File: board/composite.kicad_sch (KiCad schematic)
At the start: 17 parts, among them J6 COMPOSITE, U17 ATF1508ASx-xxJx84, U18 74HC373, U19 74HC373, U20 74HC165, U21 74HC165, Y3 14.318 MHz

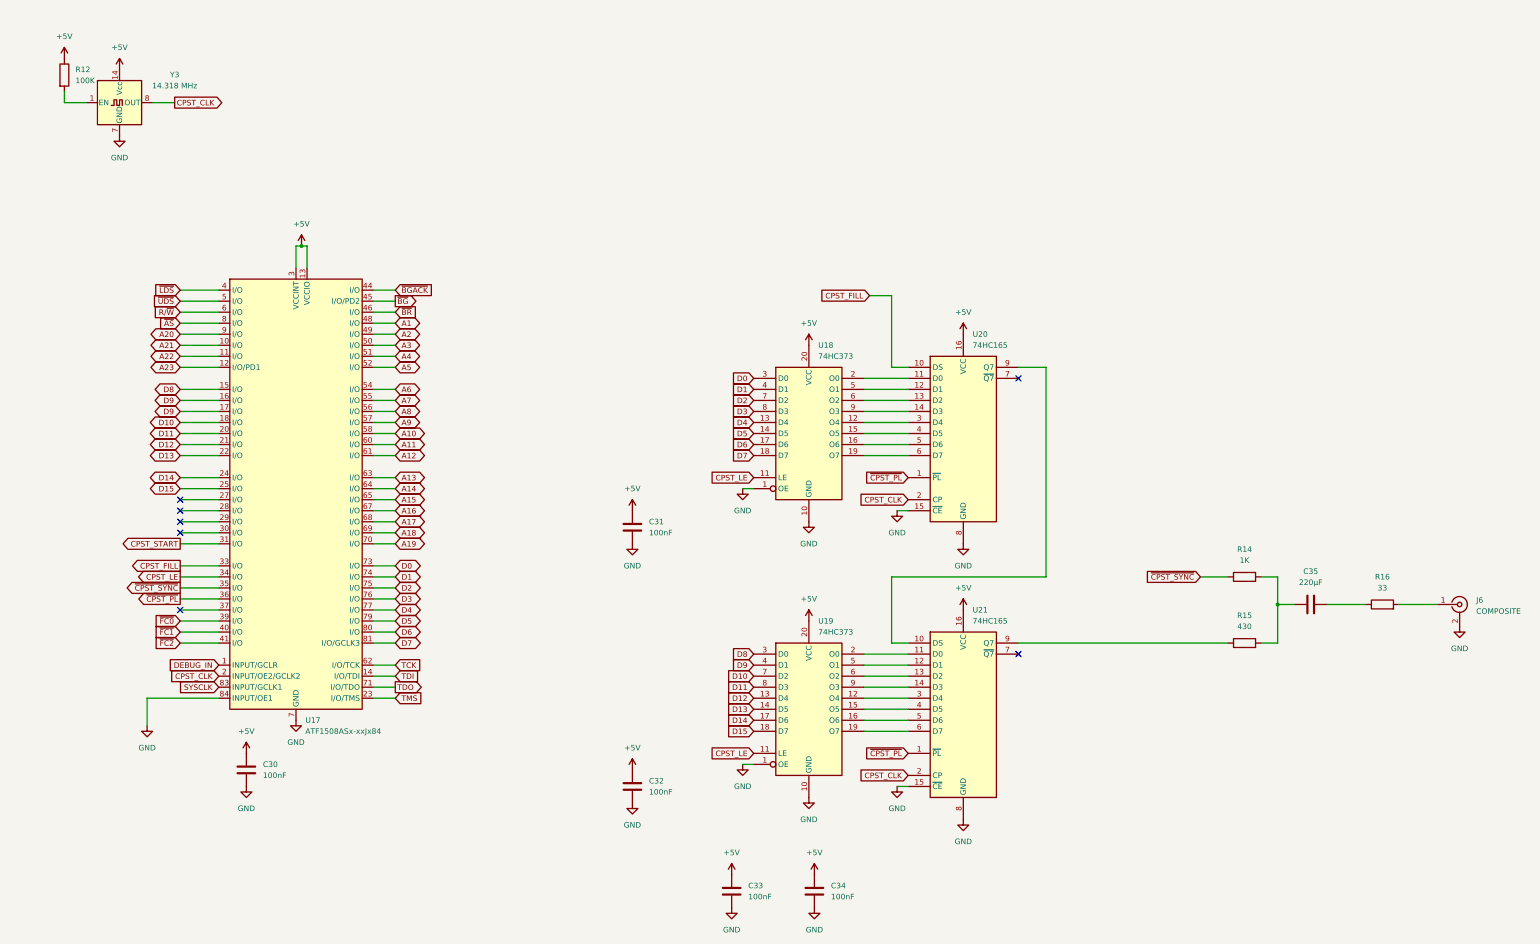
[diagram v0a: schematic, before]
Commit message: change IO to 8051 variant, add audio
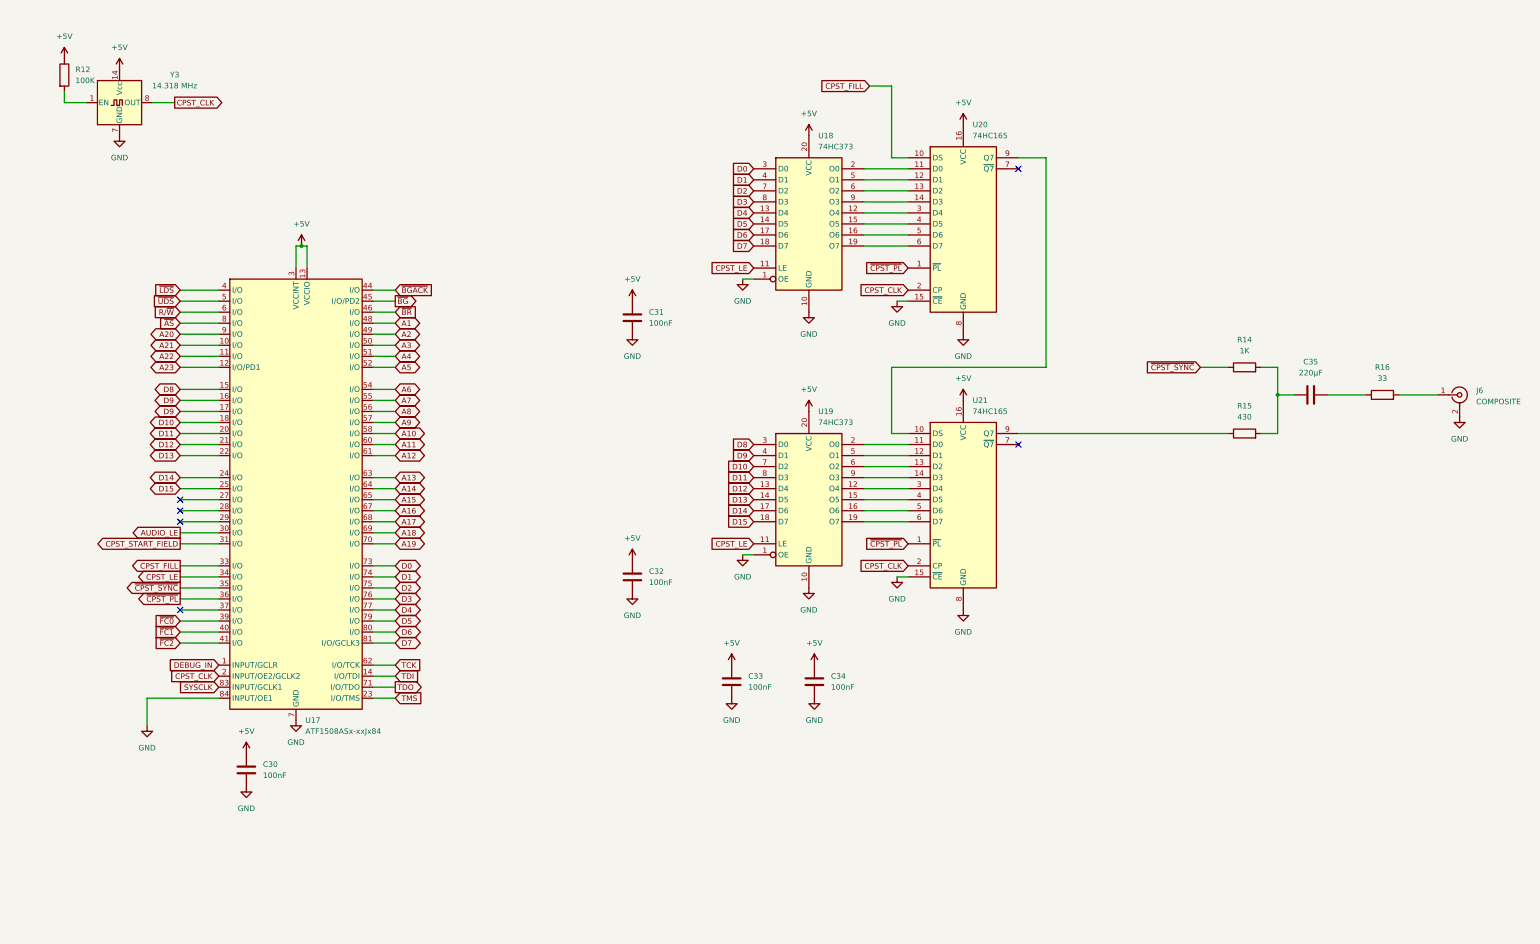
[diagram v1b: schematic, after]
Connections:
- net AUDIO_LE: now reaches U17.30 (I/O)
- net CPST_START renamed CPST_START_FIELD
- no-connect marks 7 -> 6
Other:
- moved on the sheet: C31, C32, C33, C34, C35, J6, R14, R15, R16, U18, U19, U20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

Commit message: design draft complete, added footprints
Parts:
- C30, C31, C32, C33, C34: footprint (none) -> Capacitor_THT:C_Disc_D5.0mm_W2.5mm_P5.00mm
- C35: footprint (none) -> Capacitor_THT:CP_Radial_D6.3mm_P2.50mm
- J6: footprint (none) -> board:CUI_RCJ-044
- R12, R14, R15, R16: footprint (none) -> Resistor_THT:R_Axial_DIN0207_L6.3mm_D2.5mm_P10.16mm_Horizontal
- U18, U19, U20, U21: footprint (none) -> Package_DIP:DIP-20_W7.62mm
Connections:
- net D10: now also U17.17 (I/O); no longer U17.18 (I/O)
- net D11: now also U17.18 (I/O); no longer U17.20 (I/O)
- net D12: now also U17.20 (I/O); no longer U17.21 (I/O)
- net D13: now also U17.21 (I/O); no longer U17.22 (I/O)
- net D14: now also U17.22 (I/O); no longer U17.24 (I/O)
- net D15: now also U17.24 (I/O); no longer U17.25 (I/O)
- net D9: no longer U17.17 (I/O)
- no-connect marks 6 -> 7
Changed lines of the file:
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@@
 	)
 	(no_connect
+		(at 50.8 124.46)
+	)
+	(no_connect
 		(at 50.8 127)
 	)
@@
 	(global_label "D13"
 		(shape bidirectional)
-		(at 50.8 116.84 180)
+		(at 50.8 114.3 180)
 		(fields_autoplaced yes)
 		(effects
@@
 		)
 		(property "Intersheetrefs" "${INTERSHEET_REFS}"
-			(at 44.224 116.84 0)
+			(at 44.224 114.3 0)
 			(effects
 				(font
@@
 		)
 	)
-	(global_label "D9"
-		(shape bidirectional)
-		(at 50.8 104.14 180)
-		(fields_autoplaced yes)
-		(effects
-			(font
-				(size 1.27 1.27)
-			)
-			(justify right)
-		)
-		(property "Intersheetrefs" "${INTERSHEET_REFS}"
-			(at 44.224 104.14 0)
-			(effects
-				(font
-					(size 1.27 1.27)
-				)
-				(justify right)
-				(hide yes)
-			)
-		)
-	)
 	(global_label "A18"
 		(shape bidirectional)
@@
 	(global_label "D14"
 		(shape bidirectional)
-		(at 50.8 121.92 180)
+		(at 50.8 116.84 180)
 		(fields_autoplaced yes)
 		(effects
@@
 		)
 		(property "Intersheetrefs" "${INTERSHEET_REFS}"
-			(at 44.224 121.92 0)
+			(at 44.224 116.84 0)
 			(effects
 				(font
@@
 	(global_label "D15"
 		(shape bidirectional)
-		(at 50.8 124.46 180)
+		(at 50.8 121.92 180)
 		(fields_autoplaced yes)
 		(effects
@@
 		)
 		(property "Intersheetrefs" "${INTERSHEET_REFS}"
-			(at 44.224 124.46 0)
+			(at 44.224 121.92 0)
 			(effects
 				(font
@@
 	(global_label "D11"
 		(shape bidirectional)
-		(at 50.8 111.76 180)
+		(at 50.8 109.22 180)
 		(fields_autoplaced yes)
 		(effects
@@
 		)
 		(property "Intersheetrefs" "${INTERSHEET_REFS}"
-			(at 44.224 111.76 0)
+			(at 44.224 109.22 0)
 			(effects
 				(font
@@
 	(global_label "D10"
 		(shape bidirectional)
-		(at 50.8 109.22 180)
+		(at 50.8 106.68 180)
 		(fields_autoplaced yes)
 		(effects
@@
 		)
 		(property "Intersheetrefs" "${INTERSHEET_REFS}"
-			(at 44.224 109.22 0)
+			(at 44.224 106.68 0)
 			(effects
 				(font
@@
 	(global_label "D9"
 		(shape bidirectional)
-		(at 50.8 106.68 180)
+		(at 50.8 104.14 180)
 		(fields_autoplaced yes)
 		(effects
@@
 		)
 		(property "Intersheetrefs" "${INTERSHEET_REFS}"
-			(at 44.224 106.68 0)
+			(at 44.224 104.14 0)
 			(effects
 				(font
@@
 	(global_label "D12"
 		(shape bidirectional)
-		(at 50.8 114.3 180)
+		(at 50.8 111.76 180)
 		(fields_autoplaced yes)
 		(effects
@@
 		)
 		(property "Intersheetrefs" "${INTERSHEET_REFS}"
-			(at 44.224 114.3 0)
+			(at 44.224 111.76 0)
 			(effects
 				(font
@@
 			)
 		)
-		(property "Footprint" ""
+		(property "Footprint" "Package_DIP:DIP-20_W7.62mm"
 			(at 195.58 63.5 0)
 			(effects
@@
 			)
 		)
-		(property "Footprint" ""
+		(property "Footprint" "Capacitor_THT:CP_Radial_D6.3mm_P2.50mm"
 			(at 314.96 101.9048 0)
 			(effects
@@
 			)
 		)
-		(property "Footprint" ""
+		(property "Footprint" "Resistor_THT:R_Axial_DIN0207_L6.3mm_D2.5mm_P10.16mm_Horizontal"
 			(at 295.91 113.538 90)
 			(effects
@@
 			)
 		)
-		(property "Footprint" ""
+		(property "Footprint" "Capacitor_THT:C_Disc_D5.0mm_W2.5mm_P5.00mm"
 			(at 67.0052 193.04 0)
 			(effects
@@
 			)
 		)
-		(property "Footprint" ""
+		(property "Footprint" "Resistor_THT:R_Axial_DIN0207_L6.3mm_D2.5mm_P10.16mm_Horizontal"
 			(at 327.66 104.648 90)
 			(effects
@@
 			)
 		)
-		(property "Footprint" ""
+		(property "Footprint" "Capacitor_THT:C_Disc_D5.0mm_W2.5mm_P5.00mm"
 			(at 155.9052 88.9 0)
 			(effects
@@
 			)
 		)
-		(property "Footprint" ""
+		(property "Footprint" "Package_DIP:DIP-20_W7.62mm"
 			(at 231.14 127 0)
 			(effects
@@
 			)
 		)
-		(property "Footprint" ""
+		(property "Footprint" "Package_DIP:DIP-20_W7.62mm"
 			(at 231.14 63.5 0)
 			(effects
@@
 			)
 		)
-		(property "Footprint" ""
+		(property "Footprint" "board:CUI_RCJ-044"
 			(at 345.44 102.87 0)
 			(effects
@@
 			)
 		)
-		(property "Footprint" ""
+		(property "Footprint" "Capacitor_THT:C_Disc_D5.0mm_W2.5mm_P5.00mm"
 			(at 197.8152 172.72 0)
 			(effects
@@
 			)
 		)
-		(property "Footprint" ""
+		(property "Footprint" "Package_DIP:DIP-20_W7.62mm"
 			(at 195.58 127 0)
 			(effects
@@
 			)
 		)
-		(property "Footprint" ""
+		(property "Footprint" "Resistor_THT:R_Axial_DIN0207_L6.3mm_D2.5mm_P10.16mm_Horizontal"
 			(at 295.91 98.298 90)
 			(effects
@@
 			)
 		)
-		(property "Footprint" ""
+		(property "Footprint" "Capacitor_THT:C_Disc_D5.0mm_W2.5mm_P5.00mm"
 			(at 155.9052 148.59 0)
 			(effects
@@
 			)
 		)
-		(property "Footprint" ""
+		(property "Footprint" "Resistor_THT:R_Axial_DIN0207_L6.3mm_D2.5mm_P10.16mm_Horizontal"
 			(at 22.352 29.21 90)
 			(effects
@@
 			)
 		)
-		(property "Footprint" ""
+		(property "Footprint" "Capacitor_THT:C_Disc_D5.0mm_W2.5mm_P5.00mm"
 			(at 178.7652 172.72 0)
 			(effects

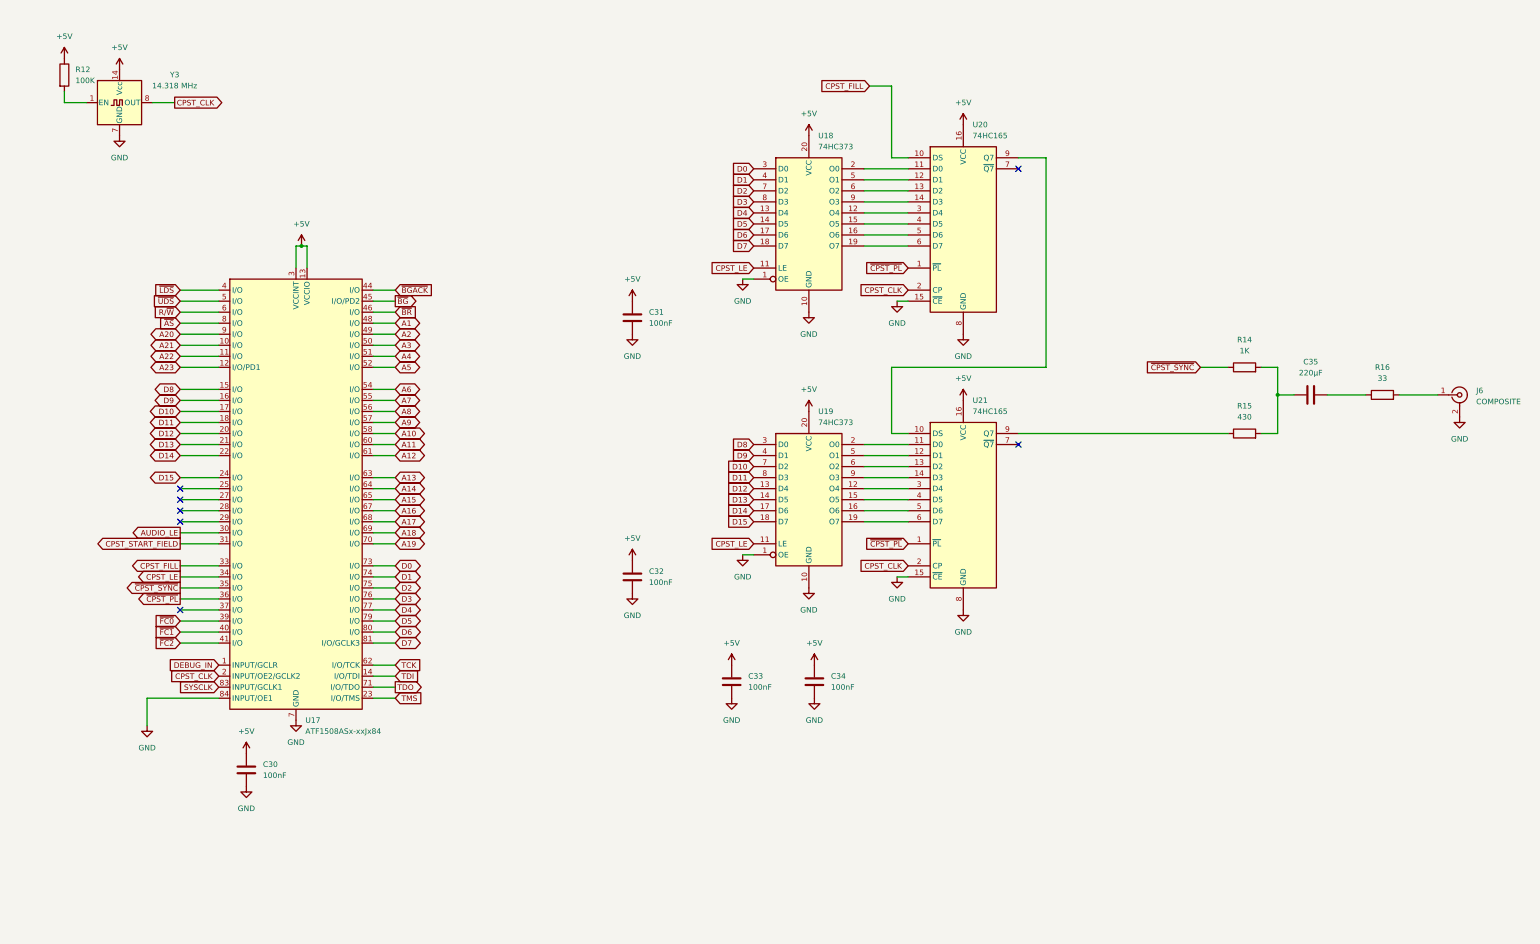
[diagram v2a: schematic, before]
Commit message: start of PCB and MMU
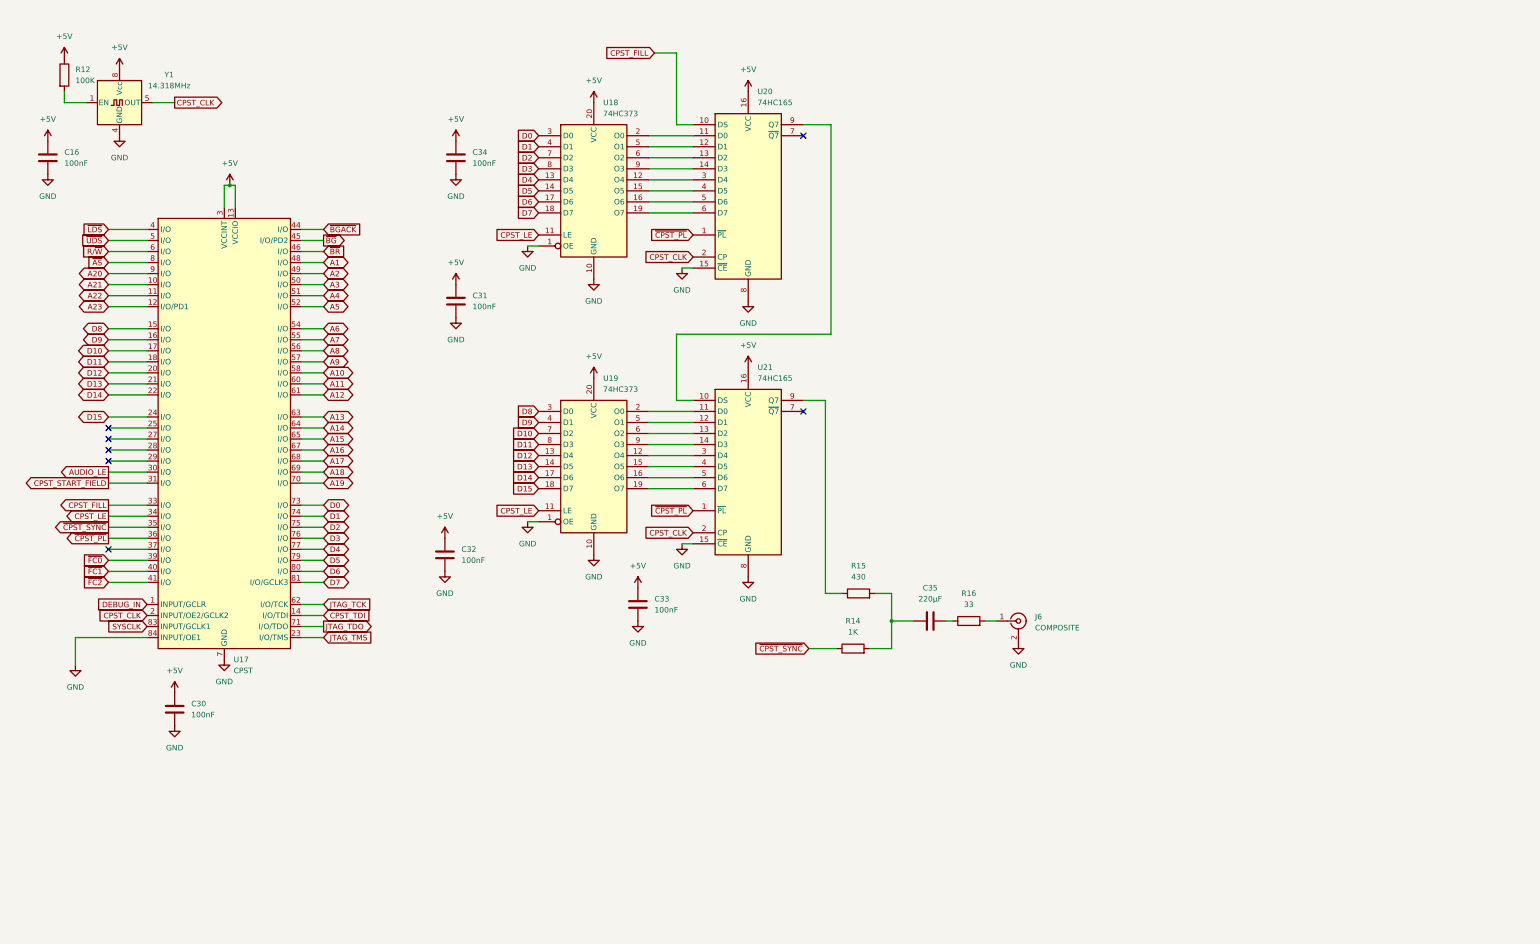
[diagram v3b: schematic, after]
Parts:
- removed Y3: 14.318 MHz, Oscillator:Oscillator_DIP-14, symbol Oscillator:CXO_DIP14
- added C16: 100nF, Capacitor_THT:C_Disc_D5.0mm_W2.5mm_P5.00mm, symbol Device:C
- added Y1: 14.318MHz, Oscillator:Oscillator_DIP-8, symbol Oscillator:CXO_DIP8
- U17: value ATF1508ASx-xxJx84 -> CPST; footprint Package_LCC:PLCC-84_29.3x29.3mm_P1.27mm -> Package_LCC:PLCC-84_THT-Socket
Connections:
- net +5V: now also C16.1, Y1.8 (Vcc)
- net CPST_CLK: now also Y1.5 (OUT)
- net GND: now also C16.2, Y1.4 (GND)
- net at R12.2: now also Y1.1 (EN)
- net TCK renamed JTAG_TCK
- net TDI renamed CPST_TDI
- net TDO renamed JTAG_TDO
- net TMS renamed JTAG_TMS
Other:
- moved on the sheet: C30, C31, C32, C33, C34, C35, J6, R14, R15, R16, U17, U18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

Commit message: checkpoint
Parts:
- U20, U21: footprint Package_DIP:DIP-20_W7.62mm -> Package_DIP:DIP-16_W7.62mm
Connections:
- net ~{CPST_DTACK}: now reaches U17.37 (I/O)
- net AUDIO_LE renamed ~{CPST_SELECT}
- no-connect marks 7 -> 6
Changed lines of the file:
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@@
 	)
 	(no_connect
-		(at 34.29 138.43)
-	)
-	(no_connect
 		(at 34.29 118.11)
 	)
@@
 		)
 	)
-	(global_label "AUDIO_LE"
-		(shape output)
-		(at 34.29 120.65 180)
-		(fields_autoplaced yes)
-		(effects
-			(font
-				(size 1.27 1.27)
-			)
-			(justify right)
-		)
-		(property "Intersheetrefs" "${INTERSHEET_REFS}"
-			(at 22.5357 120.65 0)
-			(effects
-				(font
-					(size 1.27 1.27)
-				)
-				(justify right)
-				(hide yes)
-			)
-		)
-	)
 	(global_label "CPST_TDI"
 		(shape input)
@@
 		)
 	)
+	(global_label "~{CPST_SELECT}"
+		(shape input)
+		(at 34.29 120.65 180)
+		(fields_autoplaced yes)
+		(effects
+			(font
+				(size 1.27 1.27)
+			)
+			(justify right)
+		)
+		(property "Intersheetrefs" "${INTERSHEET_REFS}"
+			(at 18.8469 120.65 0)
+			(effects
+				(font
+					(size 1.27 1.27)
+				)
+				(justify right)
+				(hide yes)
+			)
+		)
+	)
 	(global_label "D6"
 		(shape input)
@@
 		)
 	)
+	(global_label "~{CPST_DTACK}"
+		(shape output)
+		(at 34.29 138.43 180)
+		(fields_autoplaced yes)
+		(effects
+			(font
+				(size 1.27 1.27)
+			)
+			(justify right)
+		)
+		(property "Intersheetrefs" "${INTERSHEET_REFS}"
+			(at 19.7539 138.43 0)
+			(effects
+				(font
+					(size 1.27 1.27)
+				)
+				(justify right)
+				(hide yes)
+			)
+		)
+	)
 	(global_label "A16"
 		(shape bidirectional)
@@
 			)
 		)
-		(property "Footprint" "Package_DIP:DIP-20_W7.62mm"
+		(property "Footprint" "Package_DIP:DIP-16_W7.62mm"
 			(at 181.61 119.38 0)
 			(effects
@@
 			)
 		)
-		(property "Footprint" "Package_DIP:DIP-20_W7.62mm"
+		(property "Footprint" "Package_DIP:DIP-16_W7.62mm"
 			(at 181.61 55.88 0)
 			(effects

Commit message: checkpoint
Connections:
- net DEBUG_IN is gone; now on net GND: U17.1 (INPUT/GCLR)
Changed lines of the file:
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@@
 	(paper "USLetter")
+	(junction
+		(at 26.67 158.75)
+		(diameter 0)
+		(color 0 0 0 0)
+	)
 	(junction
 		(at 214.63 154.94)
@@
 	(wire
 		(pts
+			(xy 26.67 151.13) (xy 43.18 151.13)
+		)
+		(stroke
+			(width 0)
+			(type default)
+		)
+	)
+	(wire
+		(pts
 			(xy 200.66 88.9) (xy 165.1 88.9)
 		)
@@
 		(pts
 			(xy 34.29 118.11) (xy 43.18 118.11)
+		)
+		(stroke
+			(width 0)
+			(type default)
+		)
+	)
+	(wire
+		(pts
+			(xy 26.67 158.75) (xy 26.67 151.13)
 		)
 		(stroke
@@
 				(hide yes)
 			)
-		)
-	)
-	(global_label "DEBUG_IN"
-		(shape input)
-		(at 43.18 151.13 180)
-		(fields_autoplaced yes)
-		(effects
-			(font
-				(size 1.27 1.27)
-			)
-			(justify right)
-		)
-		(property "Intersheetrefs" "${INTERSHEET_REFS}"
-			(at 31.0024 151.13 0)
-			(effects
-				(font
-					(size 1.27 1.27)
-				)
-				(justify right)
-				(hide yes)
-			)
